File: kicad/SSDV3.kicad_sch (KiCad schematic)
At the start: 12 parts, among them J7 SolderPad_1x02, J8 SolderPad_1x03

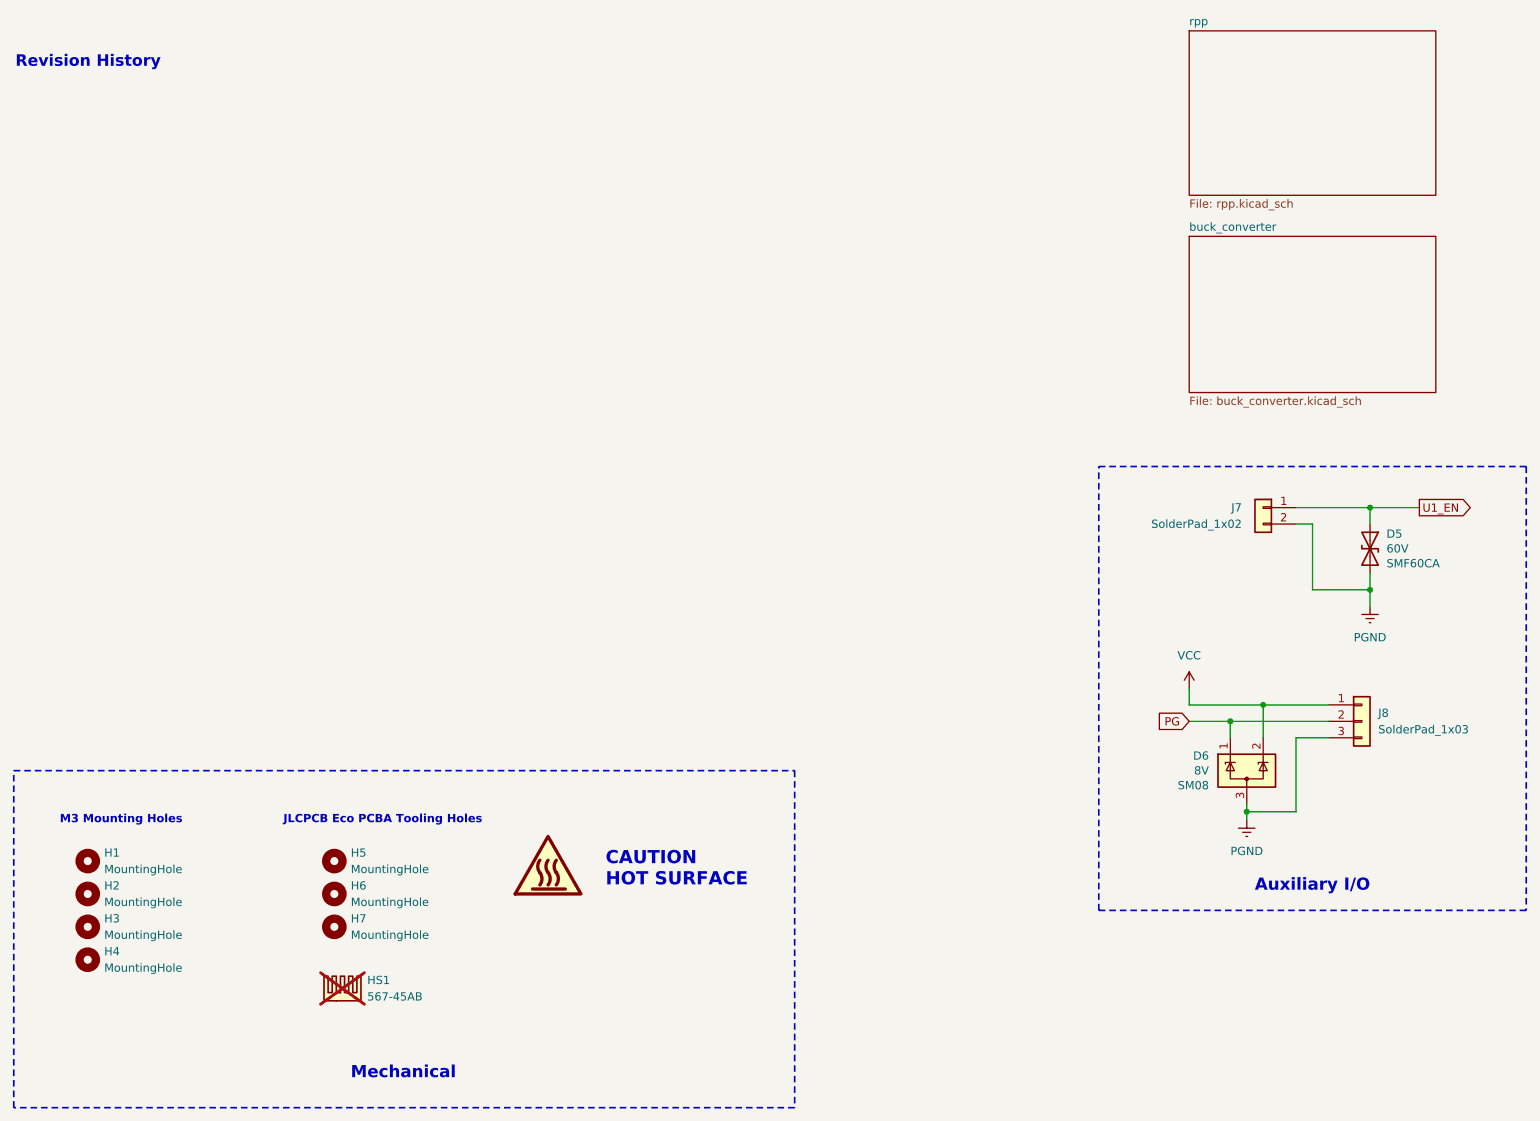
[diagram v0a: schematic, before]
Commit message: Addressed HS FET failure mode from revC
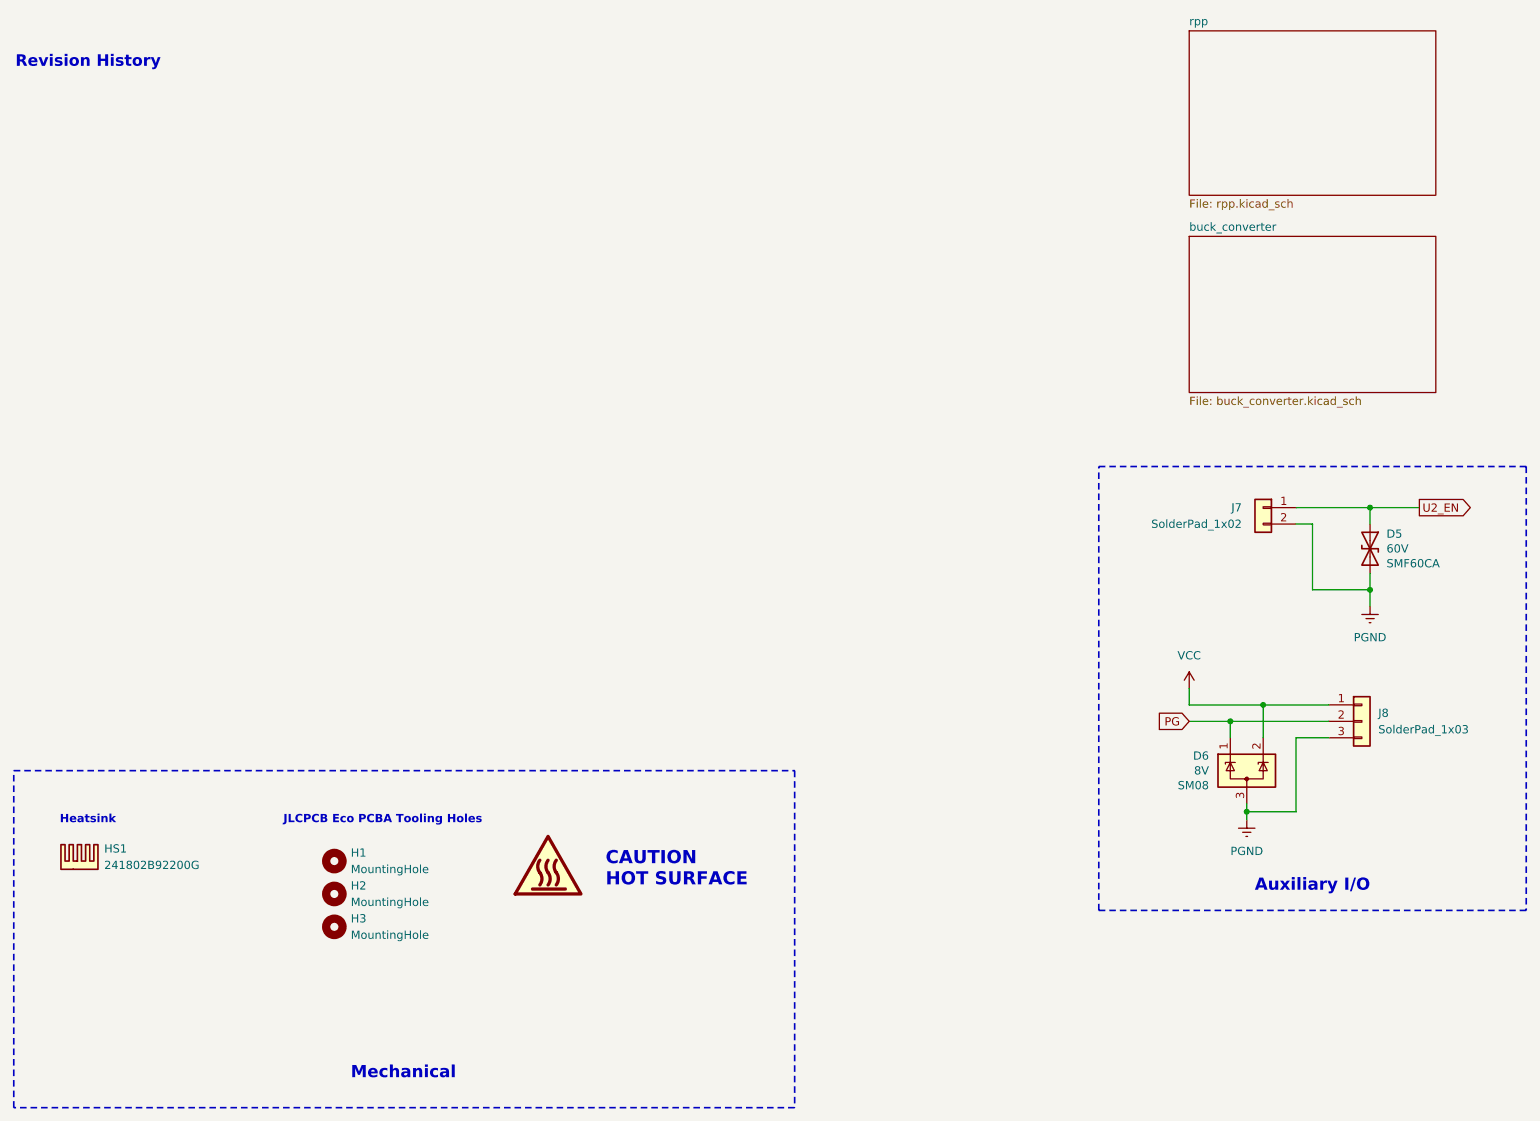
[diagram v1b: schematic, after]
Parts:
- removed H1, H2, H3, H4: MountingHole, MountingHole:MountingHole_3.2mm_M3_ISO7380, symbol Mechanical:MountingHole
- HS1: value 567-45AB -> 241802B92200G; footprint (none) -> Heatsink_JJ:24180xB9x200G; Manufacturer Wakefield-Vette -> Aavid; now fitted
- renumbered H5 to H1, H6 to H2, H7 to H3
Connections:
- net U1_EN renamed U2_EN
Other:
- note added: "Heatsink"
- note removed: "M3 Mounting Holes"
